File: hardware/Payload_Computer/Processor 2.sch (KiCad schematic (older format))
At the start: 1 part

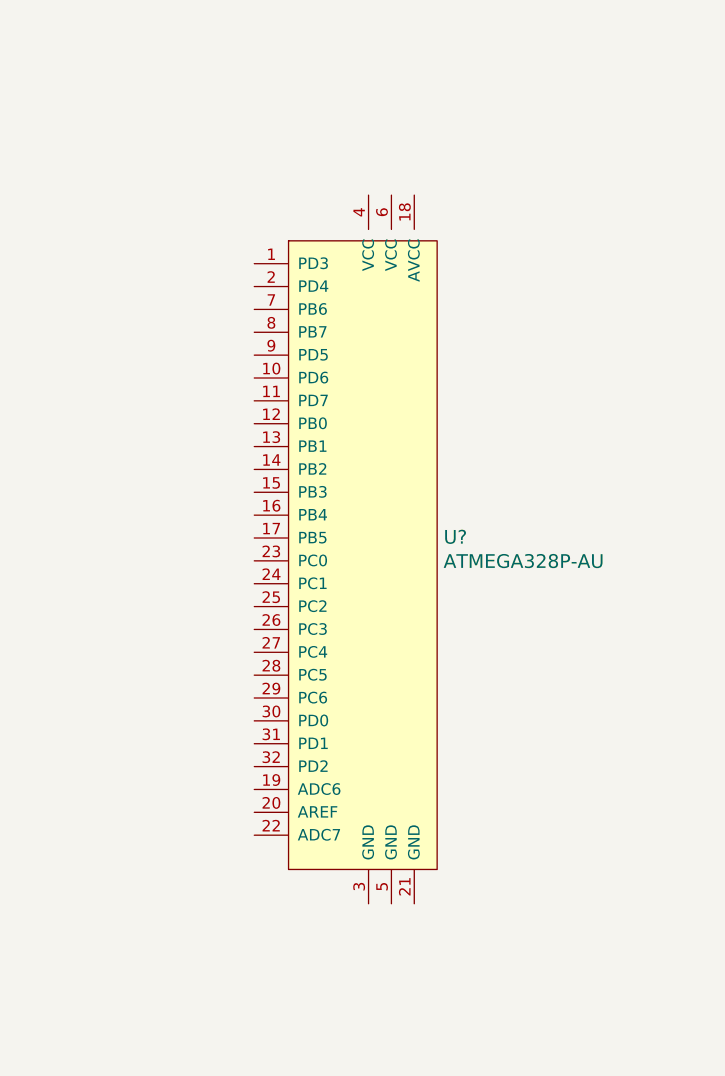
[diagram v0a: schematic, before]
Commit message: Added FTDI and crystals
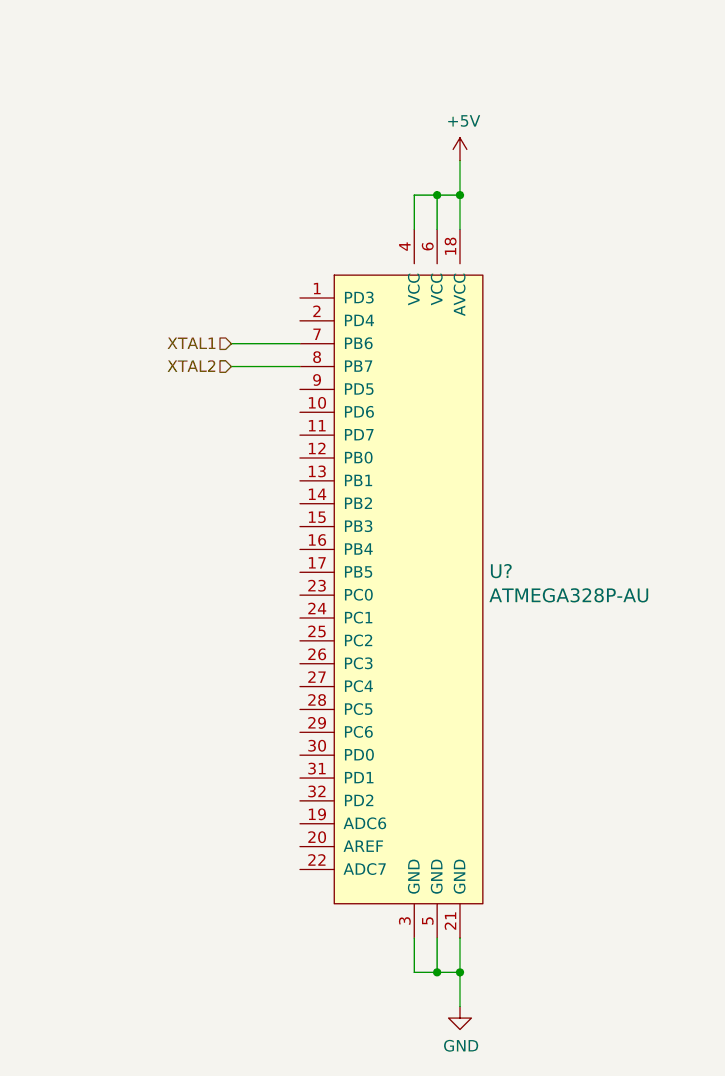
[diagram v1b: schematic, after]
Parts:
- removed U?: ATMEGA328P-AU, digikey-footprints:TQFP-32_7x7mm, symbol dk_Embedded-Microcontrollers:ATMEGA328P-AU
- added U?: ATMEGA328P-AU, digikey-footprints:TQFP-32_7x7mm, symbol dk_Embedded-Microcontrollers:ATMEGA328P-AU
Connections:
- new net +5V: U?.18 (AVCC), U?.4 (VCC), U?.6 (VCC)
- new net GND: U?.21 (GND), U?.3 (GND), U?.5 (GND)
- new net XTAL1: U?.7 (PB6)
- new net XTAL2: U?.8 (PB7)
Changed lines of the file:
@@
 $Descr A4 11693 8268
 encoding utf-8
-Sheet 3 3
+Sheet 3 6
 Title ""
 Date ""
@@
 $Comp
 L dk_Embedded-Microcontrollers:ATMEGA328P-AU U?
-U 1 1 5F847650
-P 5900 3800
-F 0 "U?" H 6228 3903 60  0000 L CNN
-F 1 "ATMEGA328P-AU" H 6228 3797 60  0000 L CNN
-F 2 "digikey-footprints:TQFP-32_7x7mm" H 6100 4000 60  0001 L CNN
-F 3 "http://www.microchip.com/mymicrochip/filehandler.aspx?ddocname=en608326" H 6100 4100 60  0001 L CNN
-F 4 "ATMEGA328P-AU-ND" H 6100 4200 60  0001 L CNN "Digi-Key_PN"
-F 5 "ATMEGA328P-AU" H 6100 4300 60  0001 L CNN "MPN"
-F 6 "Integrated Circuits (ICs)" H 6100 4400 60  0001 L CNN "Category"
-F 7 "Embedded - Microcontrollers" H 6100 4500 60  0001 L CNN "Family"
-F 8 "http://www.microchip.com/mymicrochip/filehandler.aspx?ddocname=en608326" H 6100 4600 60  0001 L CNN "DK_Datasheet_Link"
-F 9 "/product-detail/en/microchip-technology/ATMEGA328P-AU/ATMEGA328P-AU-ND/1832260" H 6100 4700 60  0001 L CNN "DK_Detail_Page"
-F 10 "IC MCU 8BIT 32KB FLASH 32TQFP" H 6100 4800 60  0001 L CNN "Description"
-F 11 "Microchip Technology" H 6100 4900 60  0001 L CNN "Manufacturer"
-F 12 "Active" H 6100 5000 60  0001 L CNN "Status"
-	1    5900 3800
+U 1 1 5F84BDD2
+P 6100 3950
+F 0 "U?" H 6428 4053 60  0000 L CNN
+F 1 "ATMEGA328P-AU" H 6428 3947 60  0000 L CNN
+F 2 "digikey-footprints:TQFP-32_7x7mm" H 6300 4150 60  0001 L CNN
+F 3 "http://www.microchip.com/mymicrochip/filehandler.aspx?ddocname=en608326" H 6300 4250 60  0001 L CNN
+F 4 "ATMEGA328P-AU-ND" H 6300 4350 60  0001 L CNN "Digi-Key_PN"
+F 5 "ATMEGA328P-AU" H 6300 4450 60  0001 L CNN "MPN"
+F 6 "Integrated Circuits (ICs)" H 6300 4550 60  0001 L CNN "Category"
+F 7 "Embedded - Microcontrollers" H 6300 4650 60  0001 L CNN "Family"
+F 8 "http://www.microchip.com/mymicrochip/filehandler.aspx?ddocname=en608326" H 6300 4750 60  0001 L CNN "DK_Datasheet_Link"
+F 9 "/product-detail/en/microchip-technology/ATMEGA328P-AU/ATMEGA328P-AU-ND/1832260" H 6300 4850 60  0001 L CNN "DK_Detail_Page"
+F 10 "IC MCU 8BIT 32KB FLASH 32TQFP" H 6300 4950 60  0001 L CNN "Description"
+F 11 "Microchip Technology" H 6300 5050 60  0001 L CNN "Manufacturer"
+F 12 "Active" H 6300 5150 60  0001 L CNN "Status"
+	1    6100 3950
 	1    0    0    -1
 $EndComp
+$Comp
+L power:+5V #PWR?
+U 1 1 5F84BDD8
+P 6300 2050
+F 0 "#PWR?" H 6300 1900 50  0001 C CNN
+F 1 "+5V" H 6315 2223 50  0000 C CNN
+F 2 "" H 6300 2050 50  0001 C CNN
+F 3 "" H 6300 2050 50  0001 C CNN
+	1    6300 2050
+	1    0    0    -1
+$EndComp
+Wire Wire Line
+	6300 2350 6300 2200
+Wire Wire Line
+	6200 2350 6200 2200
+Wire Wire Line
+	6200 2200 6300 2200
+Connection ~ 6300 2200
+Wire Wire Line
+	6300 2200 6300 2050
+Wire Wire Line
+	6100 2350 6100 2200
+Wire Wire Line
+	6100 2200 6200 2200
+Connection ~ 6200 2200
+$Comp
+L power:GND #PWR?
+U 1 1 5F84BDE6
+P 6300 5750
+F 0 "#PWR?" H 6300 5500 50  0001 C CNN
+F 1 "GND" H 6305 5577 50  0000 C CNN
+F 2 "" H 6300 5750 50  0001 C CNN
+F 3 "" H 6300 5750 50  0001 C CNN
+	1    6300 5750
+	1    0    0    -1
+$EndComp
+Wire Wire Line
+	6300 5450 6300 5600
+Wire Wire Line
+	6200 5450 6200 5600
+Wire Wire Line
+	6200 5600 6300 5600
+Connection ~ 6300 5600
+Wire Wire Line
+	6300 5600 6300 5750
+Wire Wire Line
+	6100 5450 6100 5600
+Wire Wire Line
+	6100 5600 6200 5600
+Connection ~ 6200 5600
+Text HLabel 5300 2850 0    50   Input ~ 0
+XTAL1
+Text HLabel 5300 2950 0    50   Input ~ 0
+XTAL2
+Wire Wire Line
+	5300 2850 5600 2850
+Wire Wire Line
+	5300 2950 5600 2950
 $EndSCHEMATC

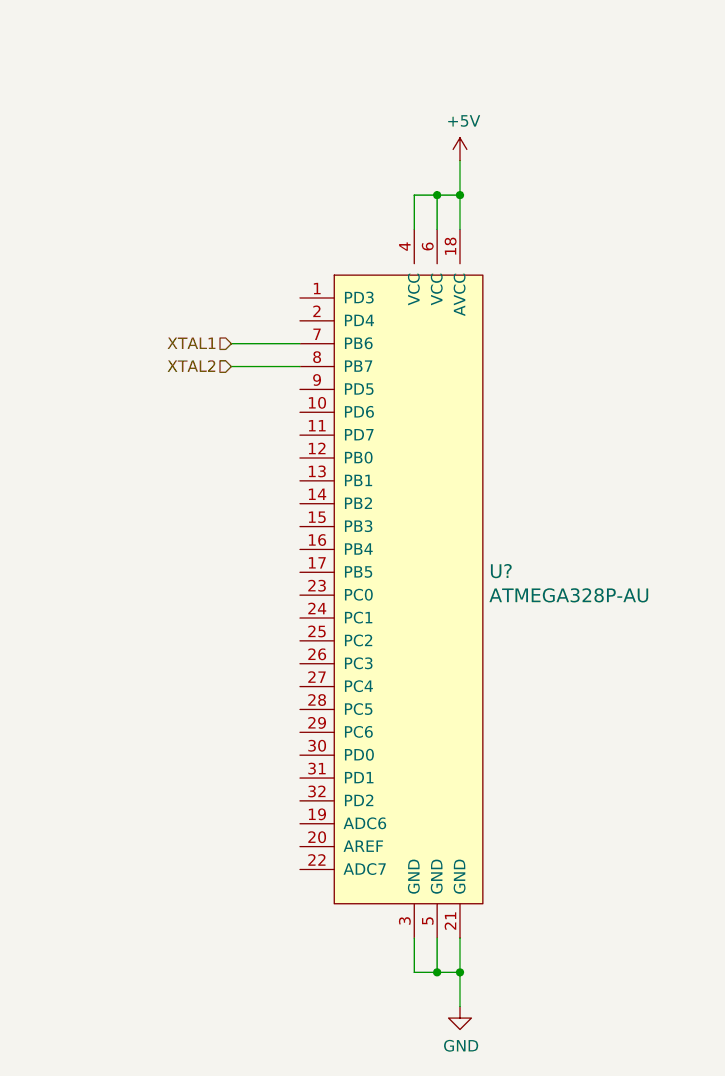
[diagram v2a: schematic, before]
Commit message: Minor updates to FTDI
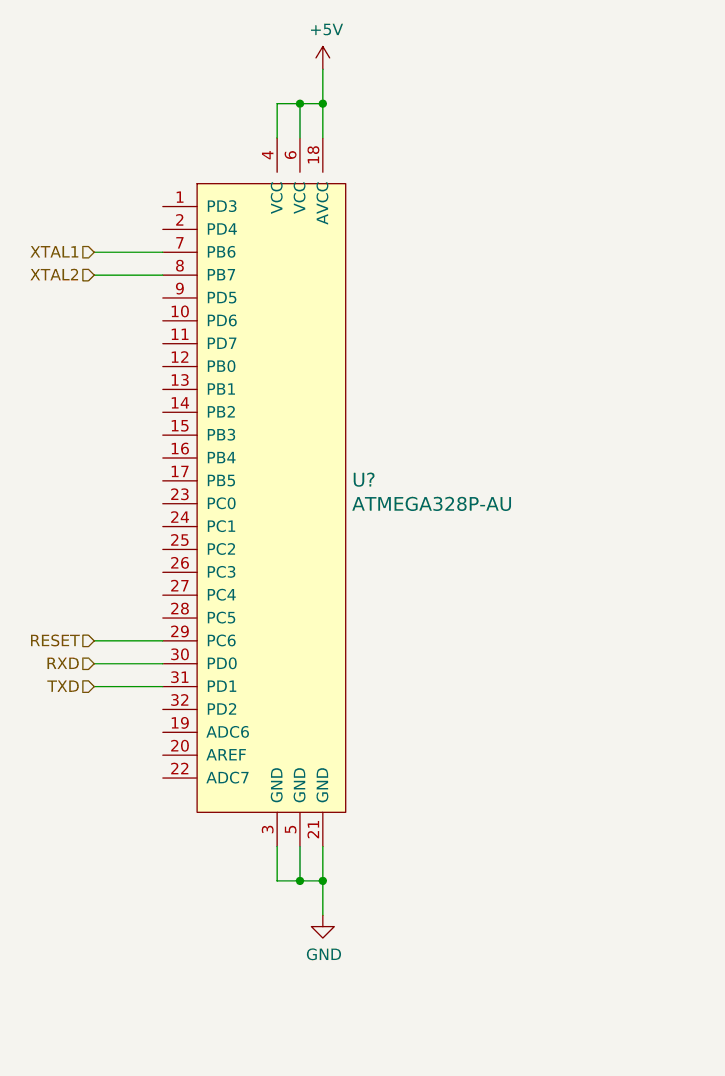
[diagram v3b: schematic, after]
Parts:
- removed U?: ATMEGA328P-AU, digikey-footprints:TQFP-32_7x7mm, symbol dk_Embedded-Microcontrollers:ATMEGA328P-AU
- added U?: ATMEGA328P-AU, digikey-footprints:TQFP-32_7x7mm, symbol dk_Embedded-Microcontrollers:ATMEGA328P-AU
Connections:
- net +5V: now also U?.18 (AVCC), U?.4 (VCC), U?.6 (VCC)
- net GND: now also U?.21 (GND), U?.3 (GND), U?.5 (GND)
- net XTAL1: now also U?.7 (PB6)
- net XTAL2: now also U?.8 (PB7)
- new net RESET: U?.29 (PC6)
- new net RXD: U?.30 (PD0)
- new net TXD: U?.31 (PD1)
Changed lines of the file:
@@
 $Comp
 L dk_Embedded-Microcontrollers:ATMEGA328P-AU U?
-U 1 1 5F84BDD2
-P 6100 3950
-F 0 "U?" H 6428 4053 60  0000 L CNN
-F 1 "ATMEGA328P-AU" H 6428 3947 60  0000 L CNN
-F 2 "digikey-footprints:TQFP-32_7x7mm" H 6300 4150 60  0001 L CNN
-F 3 "http://www.microchip.com/mymicrochip/filehandler.aspx?ddocname=en608326" H 6300 4250 60  0001 L CNN
-F 4 "ATMEGA328P-AU-ND" H 6300 4350 60  0001 L CNN "Digi-Key_PN"
-F 5 "ATMEGA328P-AU" H 6300 4450 60  0001 L CNN "MPN"
-F 6 "Integrated Circuits (ICs)" H 6300 4550 60  0001 L CNN "Category"
-F 7 "Embedded - Microcontrollers" H 6300 4650 60  0001 L CNN "Family"
-F 8 "http://www.microchip.com/mymicrochip/filehandler.aspx?ddocname=en608326" H 6300 4750 60  0001 L CNN "DK_Datasheet_Link"
-F 9 "/product-detail/en/microchip-technology/ATMEGA328P-AU/ATMEGA328P-AU-ND/1832260" H 6300 4850 60  0001 L CNN "DK_Detail_Page"
-F 10 "IC MCU 8BIT 32KB FLASH 32TQFP" H 6300 4950 60  0001 L CNN "Description"
-F 11 "Microchip Technology" H 6300 5050 60  0001 L CNN "Manufacturer"
-F 12 "Active" H 6300 5150 60  0001 L CNN "Status"
-	1    6100 3950
+U 1 1 5F8DCE4B
+P 5500 3550
+F 0 "U?" H 5828 3653 60  0000 L CNN
+F 1 "ATMEGA328P-AU" H 5828 3547 60  0000 L CNN
+F 2 "digikey-footprints:TQFP-32_7x7mm" H 5700 3750 60  0001 L CNN
+F 3 "http://www.microchip.com/mymicrochip/filehandler.aspx?ddocname=en608326" H 5700 3850 60  0001 L CNN
+F 4 "ATMEGA328P-AU-ND" H 5700 3950 60  0001 L CNN "Digi-Key_PN"
+F 5 "ATMEGA328P-AU" H 5700 4050 60  0001 L CNN "MPN"
+F 6 "Integrated Circuits (ICs)" H 5700 4150 60  0001 L CNN "Category"
+F 7 "Embedded - Microcontrollers" H 5700 4250 60  0001 L CNN "Family"
+F 8 "http://www.microchip.com/mymicrochip/filehandler.aspx?ddocname=en608326" H 5700 4350 60  0001 L CNN "DK_Datasheet_Link"
+F 9 "/product-detail/en/microchip-technology/ATMEGA328P-AU/ATMEGA328P-AU-ND/1832260" H 5700 4450 60  0001 L CNN "DK_Detail_Page"
+F 10 "IC MCU 8BIT 32KB FLASH 32TQFP" H 5700 4550 60  0001 L CNN "Description"
+F 11 "Microchip Technology" H 5700 4650 60  0001 L CNN "Manufacturer"
+F 12 "Active" H 5700 4750 60  0001 L CNN "Status"
+	1    5500 3550
 	1    0    0    -1
 $EndComp
 $Comp
 L power:+5V #PWR?
-U 1 1 5F84BDD8
-P 6300 2050
-F 0 "#PWR?" H 6300 1900 50  0001 C CNN
-F 1 "+5V" H 6315 2223 50  0000 C CNN
-F 2 "" H 6300 2050 50  0001 C CNN
-F 3 "" H 6300 2050 50  0001 C CNN
-	1    6300 2050
+U 1 1 5F8DCE51
+P 5700 1650
+F 0 "#PWR?" H 5700 1500 50  0001 C CNN
+F 1 "+5V" H 5715 1823 50  0000 C CNN
+F 2 "" H 5700 1650 50  0001 C CNN
+F 3 "" H 5700 1650 50  0001 C CNN
+	1    5700 1650
 	1    0    0    -1
 $EndComp
 Wire Wire Line
-	6300 2350 6300 2200
+	5700 1950 5700 1800
 Wire Wire Line
-	6200 2350 6200 2200
+	5600 1950 5600 1800
 Wire Wire Line
-	6200 2200 6300 2200
-Connection ~ 6300 2200
+	5600 1800 5700 1800
+Connection ~ 5700 1800
 Wire Wire Line
-	6300 2200 6300 2050
+	5700 1800 5700 1650
 Wire Wire Line
-	6100 2350 6100 2200
+	5500 1950 5500 1800
 Wire Wire Line
-	6100 2200 6200 2200
-Connection ~ 6200 2200
+	5500 1800 5600 1800
+Connection ~ 5600 1800
 $Comp
 L power:GND #PWR?
-U 1 1 5F84BDE6
-P 6300 5750
-F 0 "#PWR?" H 6300 5500 50  0001 C CNN
-F 1 "GND" H 6305 5577 50  0000 C CNN
-F 2 "" H 6300 5750 50  0001 C CNN
-F 3 "" H 6300 5750 50  0001 C CNN
-	1    6300 5750
+U 1 1 5F8DCE5F
+P 5700 5350
+F 0 "#PWR?" H 5700 5100 50  0001 C CNN
+F 1 "GND" H 5705 5177 50  0000 C CNN
+F 2 "" H 5700 5350 50  0001 C CNN
+F 3 "" H 5700 5350 50  0001 C CNN
+	1    5700 5350
 	1    0    0    -1
 $EndComp
 Wire Wire Line
-	6300 5450 6300 5600
+	5700 5050 5700 5200
 Wire Wire Line
-	6200 5450 6200 5600
+	5600 5050 5600 5200
 Wire Wire Line
-	6200 5600 6300 5600
-Connection ~ 6300 5600
+	5600 5200 5700 5200
+Connection ~ 5700 5200
 Wire Wire Line
-	6300 5600 6300 5750
+	5700 5200 5700 5350
 Wire Wire Line
-	6100 5450 6100 5600
+	5500 5050 5500 5200
 Wire Wire Line
-	6100 5600 6200 5600
-Connection ~ 6200 5600
-Text HLabel 5300 2850 0    50   Input ~ 0
+	5500 5200 5600 5200
+Connection ~ 5600 5200
+Text HLabel 4700 2450 0    50   Input ~ 0
 XTAL1
-Text HLabel 5300 2950 0    50   Input ~ 0
+Text HLabel 4700 2550 0    50   Input ~ 0
 XTAL2
 Wire Wire Line
-	5300 2850 5600 2850
+	4700 2450 5000 2450
 Wire Wire Line
-	5300 2950 5600 2950
+	4700 2550 5000 2550
+Text HLabel 4700 4350 0    50   Input ~ 0
+TXD
+Text HLabel 4700 4250 0    50   Input ~ 0
+RXD
+Wire Wire Line
+	4700 4250 5000 4250
+Wire Wire Line
+	4700 4350 5000 4350
+Text HLabel 4700 4150 0    50   Input ~ 0
+RESET
+Wire Wire Line
+	4700 4150 5000 4150
 $EndSCHEMATC
